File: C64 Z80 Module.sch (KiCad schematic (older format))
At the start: 20 parts, among them P1 C64-Exp-Port, Q1 2N3906, U1 74LS74, U10 74LS283, U11 74LS245, U13 Z80CPU, U14 74LS245, U2 74LS04, U3 74LS367, U4 74LS373, U5 74LS74, U6 74LS12, U7 74LS245, U9 74LS00

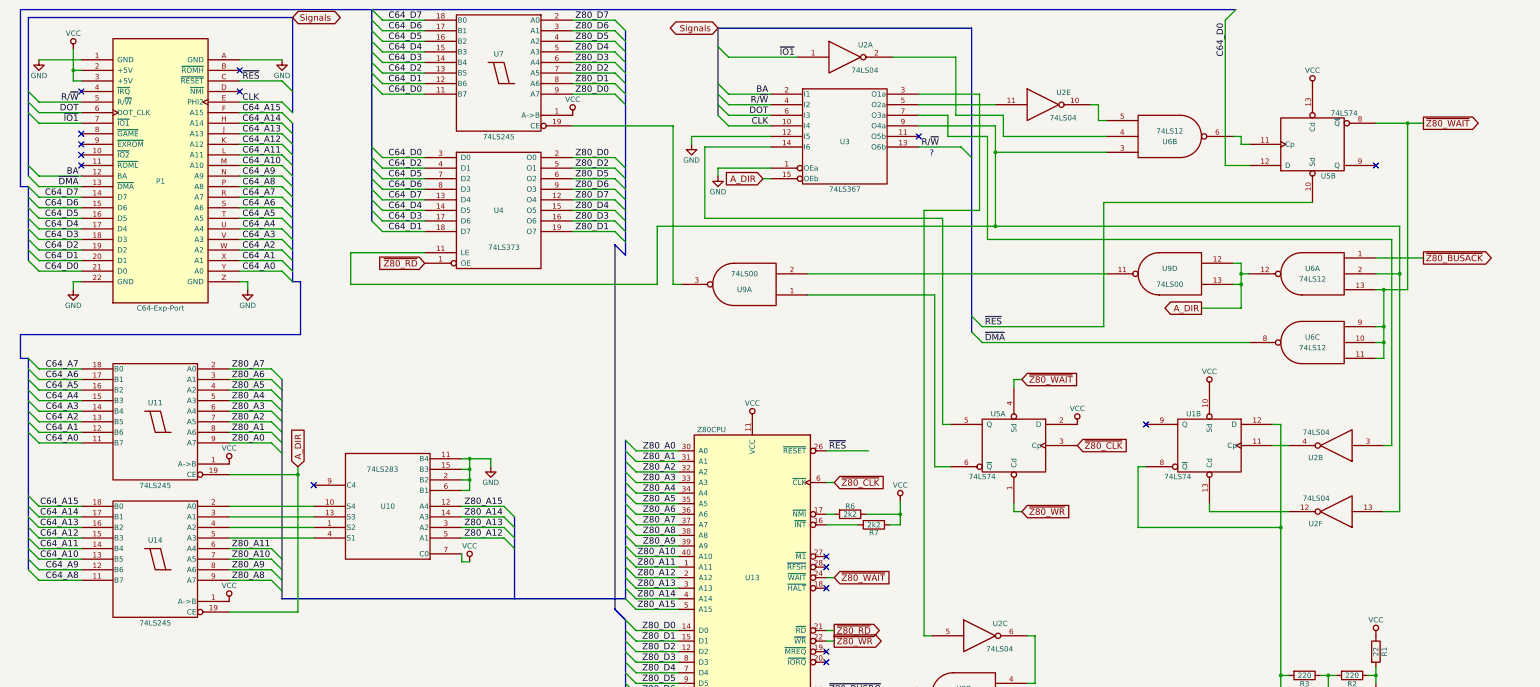
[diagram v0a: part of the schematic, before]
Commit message: Fixed errors (by ignoring them)
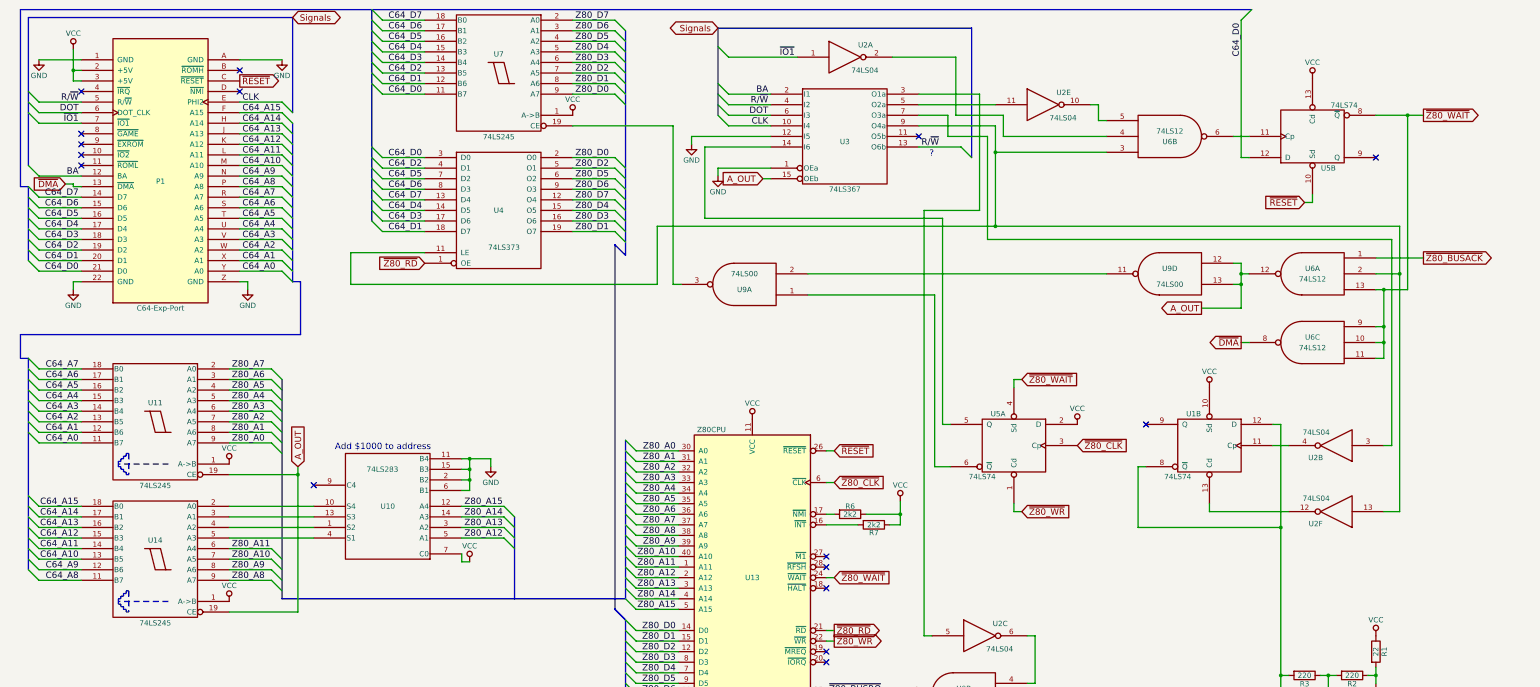
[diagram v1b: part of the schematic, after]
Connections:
- net A_DIR renamed A_OUT
- net ~RES renamed ~RESET
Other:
- note added: "Add $1000 to address"
- moved on the sheet: U5B
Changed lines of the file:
@@
 	1    0    0    -1
 $EndComp
-Text Label 3125 1325 0    60   ~ 0
-~RES
 Text Label 3125 1525 0    60   ~ 0
 CLK
@@
 Text Label 1575 2225 2    60   ~ 0
 BA
-Text Label 1575 2325 2    60   ~ 0
-~DMA
 Text Label 1575 3125 2    60   ~ 0
 C64_D0
@@
 	3500 1525 3600 1625
 Entry Wire Line
-	3500 1325 3600 1425
-Entry Wire Line
 	1100 1425 1200 1525
 Entry Wire Line
@@
 Entry Wire Line
 	1100 2125 1200 2225
-Entry Wire Line
-	1100 2225 1200 2325
 NoConn ~ 1600 1425
 NoConn ~ 1600 1825
@@
 $EndComp
 Text GLabel 3650 4975 1    60   Input ~ 0
-A_DIR
+A_OUT
 Text Label 5225 5350 0    60   ~ 0
 Z80_A15
@@
 Text GLabel 4850 3050 0    60   Input ~ 0
 ~Z80_RD
-Text Label 8675 4825 0    60   ~ 0
-~RES
 NoConn ~ 8650 6125
 NoConn ~ 8650 5925
@@
 R/~W
 Text GLabel 8050 2250 0    60   Input ~ 0
-A_DIR
+A_OUT
 NoConn ~ 9525 1850
 Text Label 8100 1750 2    60   ~ 0
@@
 	3100 1525 3500 1525
 Wire Wire Line
-	3100 1325 3500 1325
-Wire Wire Line
 	1200 1625 1600 1625
 Wire Wire Line
@@
 Wire Wire Line
 	1200 2225 1600 2225
-Wire Wire Line
-	1200 2325 1600 2325
-Wire Bus Line
-	1100 725  1100 2225
+Wire Bus Line
+	1100 725  1100 2125
 Wire Bus Line
 	1100 725  3600 725
@@
 	4350 650  4350 2650
 Wire Bus Line
-	1025 650  12525 650
+	1025 650  12675 650
 Wire Wire Line
 	6250 750  6650 750
@@
 Wire Wire Line
 	8650 6625 8725 6625
-Wire Wire Line
-	8650 4825 9050 4825
 Wire Wire Line
 	9525 1950 9925 1950
@@
 	7625 825  10025 825
 Wire Bus Line
-	10025 825  10025 3700
+	10025 825  10025 2050
 $Comp
 L 74LS04 U2
@@
 L 74LS74 U5
 U 2 1 5D1BEFF6
-P 13250 1925
-F 0 "U5" H 13400 2225 50  0000 C CNN
-F 1 "74LS74" H 13550 1630 50  0000 C CNN
-F 2 "" H 13250 1925 50  0001 C CNN
-F 3 "" H 13250 1925 50  0001 C CNN
-	2    13250 1925
+P 13250 1850
+F 0 "U5" H 13400 2150 50  0000 C CNN
+F 1 "74LS74" H 13550 1555 50  0000 C CNN
+F 2 "" H 13250 1850 50  0001 C CNN
+F 3 "" H 13250 1850 50  0001 C CNN
+	2    13250 1850
 	1    0    0    1
 $EndComp
@@
 L VCC #PWR014
 U 1 1 5D1BFC03
-P 13250 1375
-F 0 "#PWR014" H 13250 1225 50  0001 C CNN
-F 1 "VCC" H 13250 1525 50  0000 C CNN
-F 2 "" H 13250 1375 50  0001 C CNN
-F 3 "" H 13250 1375 50  0001 C CNN
-	1    13250 1375
-	1    0    0    -1
-$EndComp
-NoConn ~ 13850 2125
-Wire Wire Line
-	12500 1850 12575 1850
-Wire Wire Line
-	12575 1850 12575 1925
-Wire Wire Line
-	12575 1925 12650 1925
-Wire Wire Line
-	12425 2125 12650 2125
-Text Label 12425 775  3    60   ~ 0
+P 13250 1300
+F 0 "#PWR014" H 13250 1150 50  0001 C CNN
+F 1 "VCC" H 13250 1450 50  0000 C CNN
+F 2 "" H 13250 1300 50  0001 C CNN
+F 3 "" H 13250 1300 50  0001 C CNN
+	1    13250 1300
+	1    0    0    -1
+$EndComp
+NoConn ~ 13850 2050
+Wire Wire Line
+	12500 1850 12650 1850
+Text Label 12575 775  3    60   ~ 0
 C64_D0
 Entry Wire Line
-	12525 650  12425 750
-Wire Wire Line
-	12425 750  12425 2125
+	12675 650  12575 750
 Wire Wire Line
 	12575 3250 12500 3250
@@
 Connection ~ 13925 3650
 Wire Wire Line
-	10125 3800 12650 3800
-Wire Wire Line
-	13850 1725 14300 1725
+	13850 1650 14300 1650
 Connection ~ 13925 3300
 Wire Wire Line
@@
 	9750 2625 9750 4575
 Text GLabel 12200 3475 0    60   Output ~ 0
-A_DIR
+A_OUT
 Wire Wire Line
 	12575 3475 12200 3475
@@
 Text GLabel 11025 4775 2    60   Input ~ 0
 ~Z80_CLK
-Text Label 10150 3800 0    60   ~ 0
-~DMA
-Entry Wire Line
-	10025 3700 10125 3800
 Text Notes 9625 2050 0    60   ~ 0
 ?
@@
 Wire Wire Line
 	10625 7225 10550 7225
-Text GLabel 14300 1725 2    60   Output ~ 0
+Text GLabel 14300 1650 2    60   Output ~ 0
 ~Z80_WAIT
 Wire Wire Line
-	14150 3300 14150 1725
-Connection ~ 14150 1725
+	14150 3300 14150 1650
 $Comp
 L GND #PWR017
@@
 NoConn ~ 15300 9150
 NoConn ~ 15300 9350
-Entry Wire Line
-	10025 3550 10125 3650
-Wire Wire Line
-	10125 3650 11275 3650
-Wire Wire Line
-	11275 3650 11275 2475
-Wire Wire Line
-	11275 2475 13250 2475
-Text Label 10150 3650 0    60   ~ 0
-~RES
 NoConn ~ 13525 8700
 $Comp
@@
 Wire Wire Line
 	7050 3250 7050 2700
+Text GLabel 8725 4825 2    60   Input ~ 0
+~RESET
+Wire Wire Line
+	8725 4825 8650 4825
+Text GLabel 3100 1325 2    60   Output ~ 0
+~RESET
+Text GLabel 13175 2475 0    60   Input ~ 0
+~RESET
+Wire Wire Line
+	13250 2400 13250 2475
+Wire Wire Line
+	13250 2475 13175 2475
+Connection ~ 14150 1650
+Wire Wire Line
+	12650 2050 12575 2050
+Wire Wire Line
+	12575 2050 12575 750
+Text GLabel 1450 2300 0    60   Input ~ 0
+~DMA
+Wire Wire Line
+	1600 2325 1525 2325
+Wire Wire Line
+	1525 2325 1525 2300
+Wire Wire Line
+	1525 2300 1450 2300
+Text GLabel 12575 3800 0    60   Output ~ 0
+~DMA
+Wire Wire Line
+	12575 3800 12650 3800
+Wire Notes Line
+	2425 4950 1950 4950
+Wire Notes Line
+	1950 4925 1950 4975
+Wire Notes Line
+	1950 4925 1975 4925
+Wire Notes Line
+	1975 4925 1975 4900
+Wire Notes Line
+	1975 4900 2000 4900
+Wire Notes Line
+	2000 4900 2000 4875
+Wire Notes Line
+	2000 4875 2025 4875
+Wire Notes Line
+	2025 4875 2025 4850
+Wire Notes Line
+	2025 4850 2050 4850
+Wire Notes Line
+	2050 4850 2050 5050
+Wire Notes Line
+	1950 4975 1975 4975
+Wire Notes Line
+	1975 4975 1975 5000
+Wire Notes Line
+	1975 5000 2000 5000
+Wire Notes Line
+	2000 5000 2000 5025
+Wire Notes Line
+	2000 5025 2025 5025
+Wire Notes Line
+	2025 5025 2025 5050
+Wire Notes Line
+	2025 5050 2050 5050
+Wire Notes Line
+	2425 6250 1950 6250
+Wire Notes Line
+	1950 6225 1950 6275
+Wire Notes Line
+	1950 6225 1975 6225
+Wire Notes Line
+	1975 6225 1975 6200
+Wire Notes Line
+	1975 6200 2000 6200
+Wire Notes Line
+	2000 6200 2000 6175
+Wire Notes Line
+	2000 6175 2025 6175
+Wire Notes Line
+	2025 6175 2025 6150
+Wire Notes Line
+	2025 6150 2050 6150
+Wire Notes Line
+	2050 6150 2050 6350
+Wire Notes Line
+	1950 6275 1975 6275
+Wire Notes Line
+	1975 6275 1975 6300
+Wire Notes Line
+	1975 6300 2000 6300
+Wire Notes Line
+	2000 6300 2000 6325
+Wire Notes Line
+	2000 6325 2025 6325
+Wire Notes Line
+	2025 6325 2025 6350
+Wire Notes Line
+	2025 6350 2050 6350
+Text Notes 4000 4825 0    60   ~ 0
+Add $1000 to address
 $EndSCHEMATC

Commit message: Added notes to schematic for easier read
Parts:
- removed U3: 74LS367, symbol 74LS367
- added C1, C10, C11, C2, C3, C4, C5, C6, C7, C8: 100nF, symbol C_Small
- added U3: 74LS367, symbol 74LS367_ab_fix
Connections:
- net A_OUT: now also U3.15 (OEb)
- net BA: now also U3.2 (I1)
- net CLK: now also U3.10 (I4)
- net DOT: now also U3.6 (I3)
- net GND: now also U9.10, U9.9, C1.2, C10.2, C11.2, C2.2, C3.2, C4.2, C5.2, C6.2, C7.2, C8.2, U3.1 (OEa), U3.12 (I5), U3.8 (GND)
- net R/~W: now also U3.13 (O6b), U3.4 (I2)
- net VCC: now also U1.1 (Cd), U1.2 (D), U1.3 (Cp), U1.4 (Sd), C1.1, C10.1, C11.1, C2.1, C3.1, C4.1, C5.1, C6.1, C7.1, C8.1, U3.16 (VCC)
- net D_OUT: now reaches U7.19 (CE), U9.3
- net Z80_R/~W: now reaches U5.5 (Q)
- net Z80_R/~W: now also U3.14 (I6)
- net at U2.5: now also U3.3 (O1a)
- net at U2.11: now also U3.5 (O2a)
- net at U2.3: now also U3.7 (O3a)
- net at U2.13, U4.11 (LE), U6.2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: now also U3.9 (O4b)
- net C64_D0 renamed D0
- no-connect marks 25 -> 19
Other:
- note added: "8Mhz DOT clock divide by two,\ncombine with Phi2 to reduce duty\ncycle. Needed in order to allow \nstock components a chance to\nrespond. 3Mhz Z80 clock, \nwith 3-4 CPU cycles compared to\n6502 the result is 1Mhz."
- note added: "Activate Z80 module from 6510\nby writing $0 to $DE00"
- note added: "Attempts to clean up edges of the clock,\nI think though this have to be compared\nwith oscilloscope readings."
- note added: "Based on the Commodore 64 CP/M cartridge, as detailed and sketched out by Ruud\nBaltissen. In essence, "stolen from Ruud" with the hope of making something out of it."
- note added: "Ensure data is not written to bus\nduring Z80/6510 control transition,\nguesstimating."
- note added: "Halts 6510\non Z80 enable"
- note added: "VIC requests bus access (BA)"
- note removed: "?"
- moved on the sheet: U1A, U1B, U2B, U2F, U5A, U9A, U9C

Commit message: Assigned footprints
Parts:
- C1, C10, C11, C2, C3, C4, C5, C6, C7, C8, C9: footprint (none) -> Capacitors_THT:C_Disc_D4.7mm_W2.5mm_P5.00mm
- P1: footprint MODULE -> C64-Exp-Port:C64-Cart
- Q1: footprint TO_SOT_Packages_THT:TO-92_Molded_Narrow -> TO_SOT_Packages_THT:TO-92_Inline_Wide
- R1, R2, R3, R6, R7: footprint (none) -> Resistors_THT:R_Axial_DIN0207_L6.3mm_D2.5mm_P10.16mm_Horizontal
- U1, U2, U5, U6, U9: footprint (none) -> Housings_DIP:DIP-14_W7.62mm_Socket
- U10, U3: footprint (none) -> Housings_DIP:DIP-16_W7.62mm_Socket
- U11, U14, U4, U7: footprint (none) -> Housings_DIP:DIP-20_W7.62mm_Socket
- U13: footprint (none) -> Housings_DIP:DIP-40_W15.24mm_Socket

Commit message: Layout done
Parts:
- added C1, C2: 100nF, Capacitors_THT:C_Disc_D4.7mm_W2.5mm_P5.00mm, symbol C_Small
- added D1: WAIT_LED, LEDs:LED_D5.0mm, symbol LED
- added R4: 220, Resistors_THT:R_Axial_DIN0207_L6.3mm_D2.5mm_P10.16mm_Horizontal, symbol R
- renumbered C1 to C13, C2 to C14
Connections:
- net GND: now also C9.2, C1.2, C2.2, D1.1 (K); no longer C8.2
- net VCC: now also C9.1, C1.1, C2.1; no longer C8.1
- net ~Z80_WAIT: now also R4.2
- net at U1.12 (D), U1.8 (~Q), U2.9: now also C8.2, R3.1; no longer C9.2, R3.2
- net at Q1.2 (B), R2.2: now also C8.1, R3.2; no longer C9.1, R3.1
- new net: D1.2 (A), R4.1
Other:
- moved on the sheet: C8, C9
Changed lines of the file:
@@
 Connection ~ 13925 3650
 Wire Wire Line
-	13850 1650 14300 1650
+	13850 1650 15275 1650
 Connection ~ 13925 3300
 Wire Wire Line
@@
 Wire Wire Line
 	10625 7225 10550 7225
-Text GLabel 14300 1650 2    60   Output ~ 0
+Text GLabel 15275 1650 2    60   Output ~ 0
 ~Z80_WAIT
 Wire Wire Line
@@
 F 3 "" H 13175 6950 50  0001 C CNN
 	1    13175 6950
-	0    1    1    0
+	0    -1   -1   0
 $EndComp
 $Comp
@@
 L C_Small C9
 U 1 1 5D1E7718
-P 13175 7225
-F 0 "C9" H 13185 7295 50  0000 L CNN
-F 1 "100nF" H 13185 7145 50  0000 L CNN
-F 2 "Capacitors_THT:C_Disc_D4.7mm_W2.5mm_P5.00mm" H 13175 7225 50  0001 C CNN
-F 3 "" H 13175 7225 50  0001 C CNN
-	1    13175 7225
-	0    1    1    0
+P 2750 10650
+F 0 "C9" H 2760 10720 50  0000 L CNN
+F 1 "100nF" H 2760 10570 50  0000 L CNN
+F 2 "Capacitors_THT:C_Disc_D4.7mm_W2.5mm_P5.00mm" H 2750 10650 50  0001 C CNN
+F 3 "" H 2750 10650 50  0001 C CNN
+	1    2750 10650
+	1    0    0    -1
 $EndComp
 Connection ~ 12950 6950
@@
 Connection ~ 10925 10150
 $Comp
-L C_Small C1
+L C_Small C13
 U 1 1 5D26F128
 P 825 10650
-F 0 "C1" H 835 10720 50  0000 L CNN
+F 0 "C13" H 835 10720 50  0000 L CNN
 F 1 "100nF" H 835 10570 50  0000 L CNN
 F 2 "Capacitors_THT:C_Disc_D4.7mm_W2.5mm_P5.00mm" H 825 10650 50  0001 C CNN
@@
 $EndComp
 $Comp
-L C_Small C2
+L C_Small C14
 U 1 1 5D26F60D
 P 1100 10650
-F 0 "C2" H 1110 10720 50  0000 L CNN
+F 0 "C14" H 1110 10720 50  0000 L CNN
 F 1 "100nF" H 1110 10570 50  0000 L CNN
 F 2 "Capacitors_THT:C_Disc_D4.7mm_W2.5mm_P5.00mm" H 1100 10650 50  0001 C CNN
@@
 L C_Small C8
 U 1 1 5D26FDCC
-P 2750 10650
-F 0 "C8" H 2760 10720 50  0000 L CNN
-F 1 "100nF" H 2760 10570 50  0000 L CNN
-F 2 "Capacitors_THT:C_Disc_D4.7mm_W2.5mm_P5.00mm" H 2750 10650 50  0001 C CNN
-F 3 "" H 2750 10650 50  0001 C CNN
-	1    2750 10650
-	1    0    0    -1
+P 13175 7225
+F 0 "C8" H 13185 7295 50  0000 L CNN
+F 1 "100nF" H 13185 7145 50  0000 L CNN
+F 2 "Capacitors_THT:C_Disc_D4.7mm_W2.5mm_P5.00mm" H 13175 7225 50  0001 C CNN
+F 3 "" H 13175 7225 50  0001 C CNN
+	1    13175 7225
+	0    1    1    0
 $EndComp
 $Comp
@@
 	825  10400 825  10550
 Wire Wire Line
-	3300 10825 825  10825
+	825  10825 3850 10825
 Wire Wire Line
 	825  10825 825  10750
@@
 Connection ~ 3025 10825
 Wire Wire Line
-	825  10475 3300 10475
+	825  10475 3850 10475
 Wire Wire Line
 	1100 10475 1100 10550
@@
 	1    0    0    -1
 $EndComp
+$Comp
+L C_Small C2
+U 1 1 5D1C483B
+P 3575 10650
+F 0 "C2" H 3585 10720 50  0000 L CNN
+F 1 "100nF" H 3585 10570 50  0000 L CNN
+F 2 "Capacitors_THT:C_Disc_D4.7mm_W2.5mm_P5.00mm" H 3575 10650 50  0001 C CNN
+F 3 "" H 3575 10650 50  0001 C CNN
+	1    3575 10650
+	1    0    0    -1
+$EndComp
+Wire Wire Line
+	3575 10475 3575 10550
+Connection ~ 3300 10475
+Wire Wire Line
+	3575 10825 3575 10750
+$Comp
+L C_Small C1
+U 1 1 5D1C57A4
+P 3850 10650
+F 0 "C1" H 3860 10720 50  0000 L CNN
+F 1 "100nF" H 3860 10570 50  0000 L CNN
+F 2 "Capacitors_THT:C_Disc_D4.7mm_W2.5mm_P5.00mm" H 3850 10650 50  0001 C CNN
+F 3 "" H 3850 10650 50  0001 C CNN
+	1    3850 10650
+	1    0    0    -1
+$EndComp
+Wire Wire Line
+	3850 10475 3850 10550
+Connection ~ 3575 10475
+Wire Wire Line
+	3850 10825 3850 10750
+Connection ~ 3575 10825
+$Comp
+L R R4
+U 1 1 5D1C9B49
+P 15100 1425
+F 0 "R4" V 15180 1425 50  0000 C CNN
+F 1 "220" V 15100 1425 50  0000 C CNN
+F 2 "Resistors_THT:R_Axial_DIN0207_L6.3mm_D2.5mm_P10.16mm_Horizontal" V 15030 1425 50  0001 C CNN
+F 3 "" H 15100 1425 50  0001 C CNN
+	1    15100 1425
+	1    0    0    -1
+$EndComp
+$Comp
+L LED D1
+U 1 1 5D1CA3F0
+P 15100 1050
+F 0 "D1" H 15100 1150 50  0000 C CNN
+F 1 "WAIT_LED" H 15100 925 50  0000 C CNN
+F 2 "LEDs:LED_D5.0mm" H 15100 1050 50  0001 C CNN
+F 3 "" H 15100 1050 50  0001 C CNN
+	1    15100 1050
+	0    1    1    0
+$EndComp
+Wire Wire Line
+	15100 1575 15100 1650
+Connection ~ 15100 1650
+Wire Wire Line
+	15100 1200 15100 1275
+$Comp
+L GND #PWR024
+U 1 1 5D1CB01D
+P 15325 900
+F 0 "#PWR024" H 15325 650 50  0001 C CNN
+F 1 "GND" H 15325 750 50  0000 C CNN
+F 2 "" H 15325 900 50  0001 C CNN
+F 3 "" H 15325 900 50  0001 C CNN
+	1    15325 900
+	1    0    0    -1
+$EndComp
+Wire Wire Line
+	15100 900  15100 825
+Wire Wire Line
+	15100 825  15325 825
+Wire Wire Line
+	15325 825  15325 900
 $EndSCHEMATC
